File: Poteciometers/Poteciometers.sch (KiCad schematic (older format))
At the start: 14 parts, among them J1 POT_PMOD, J2 EXT_PMOD

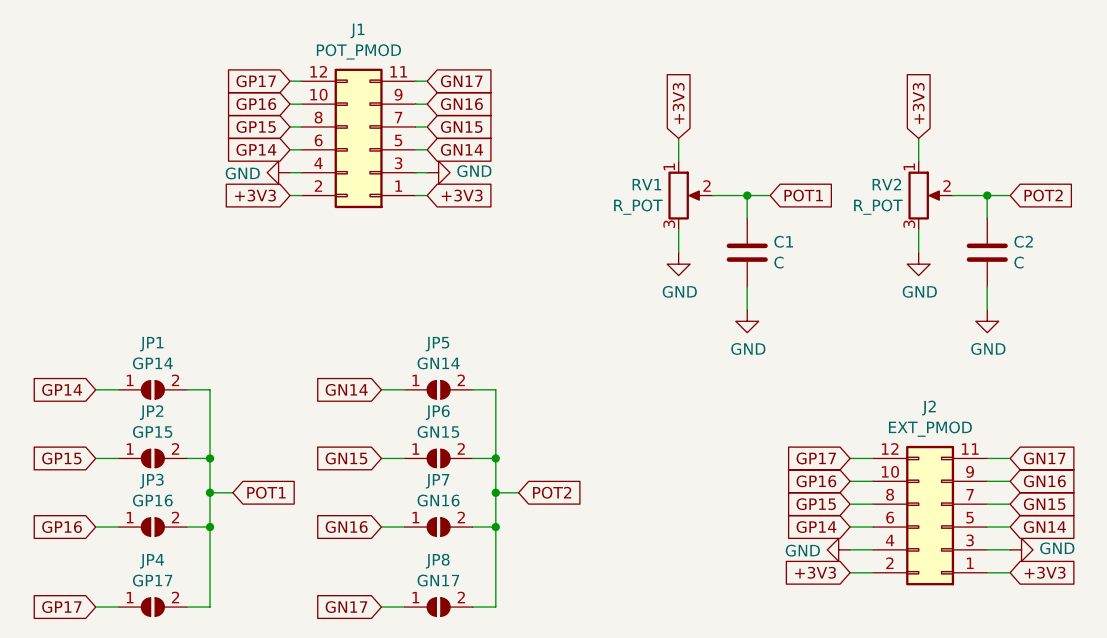
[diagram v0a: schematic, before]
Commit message: Adding shift by one suggested by tnt
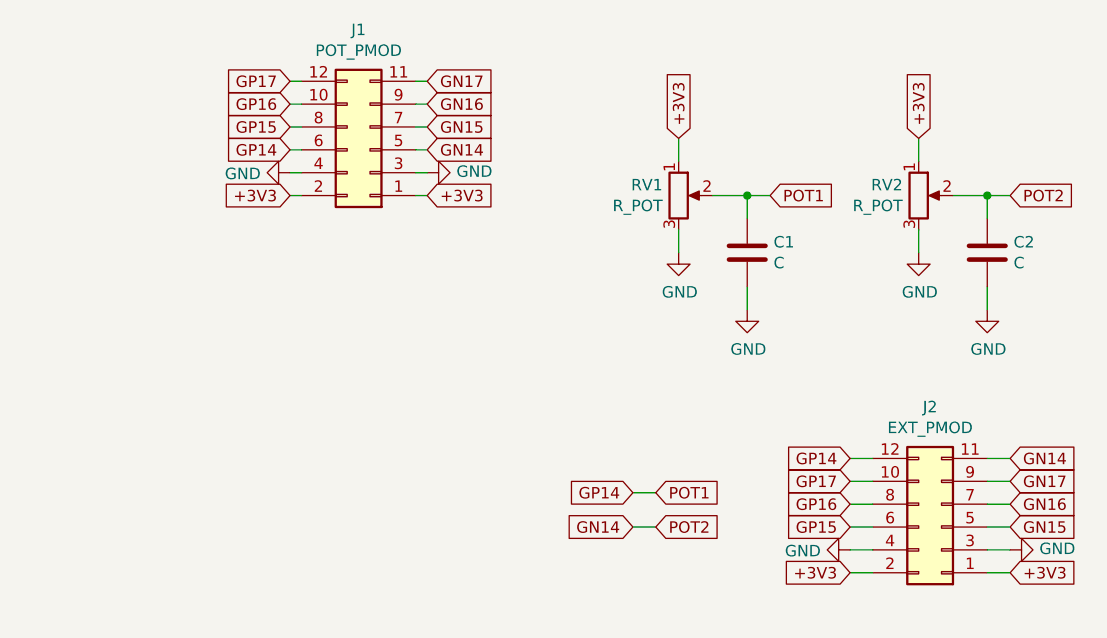
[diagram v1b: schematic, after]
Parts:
- removed JP1: GP14, Jumper:SolderJumper-2_P1.3mm_Open_TrianglePad1.0x1.5mm, symbol Jumper:SolderJumper_2_Open
- removed JP2: GP15, Jumper:SolderJumper-2_P1.3mm_Open_TrianglePad1.0x1.5mm, symbol Jumper:SolderJumper_2_Open
- removed JP3: GP16, Jumper:SolderJumper-2_P1.3mm_Open_TrianglePad1.0x1.5mm, symbol Jumper:SolderJumper_2_Open
- removed JP4: GP17, Jumper:SolderJumper-2_P1.3mm_Open_TrianglePad1.0x1.5mm, symbol Jumper:SolderJumper_2_Open
- removed JP5: GN14, Jumper:SolderJumper-2_P1.3mm_Open_TrianglePad1.0x1.5mm, symbol Jumper:SolderJumper_2_Open
- removed JP6: GN15, Jumper:SolderJumper-2_P1.3mm_Open_TrianglePad1.0x1.5mm, symbol Jumper:SolderJumper_2_Open
- removed JP7: GN16, Jumper:SolderJumper-2_P1.3mm_Open_TrianglePad1.0x1.5mm, symbol Jumper:SolderJumper_2_Open
- removed JP8: GN17, Jumper:SolderJumper-2_P1.3mm_Open_TrianglePad1.0x1.5mm, symbol Jumper:SolderJumper_2_Open
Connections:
- net POT1 is gone; now on net GP14: C1.1, RV1.2
- net POT2 is gone; now on net GN14: C2.1, RV2.2
- net GN14: now also J2.11 (Pin_11); no longer J2.5 (Pin_5)
- net GN15: now also J2.5 (Pin_5); no longer J2.7 (Pin_7)
- net GN16: now also J2.7 (Pin_7); no longer J2.9 (Pin_9)
- net GN17: now also J2.9 (Pin_9); no longer J2.11 (Pin_11)
- net GP14: now also J2.12 (Pin_12); no longer J2.6 (Pin_6)
- net GP15: now also J2.6 (Pin_6); no longer J2.8 (Pin_8)
- net GP16: now also J2.8 (Pin_8); no longer J2.10 (Pin_10)
- net GP17: now also J2.10 (Pin_10); no longer J2.12 (Pin_12)
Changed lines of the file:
@@
 Wire Wire Line
 	5100 1900 5100 1800
-$Comp
-L Jumper:SolderJumper_2_Open JP1
-U 1 1 5E8A5DA7
-P 1450 2250
-F 0 "JP1" H 1450 2455 50  0000 C CNN
-F 1 "GP14" H 1450 2364 50  0000 C CNN
-F 2 "Jumper:SolderJumper-2_P1.3mm_Open_TrianglePad1.0x1.5mm" H 1450 2250 50  0001 C CNN
-F 3 "~" H 1450 2250 50  0001 C CNN
-	1    1450 2250
-	1    0    0    -1
-$EndComp
-Text GLabel 1800 2700 2    50   Input ~ 0
+Text GLabel 3650 2700 2    50   Input ~ 0
 POT1
-$Comp
-L Jumper:SolderJumper_2_Open JP2
-U 1 1 5E8A617E
-P 1450 2550
-F 0 "JP2" H 1450 2755 50  0000 C CNN
-F 1 "GP15" H 1450 2664 50  0000 C CNN
-F 2 "Jumper:SolderJumper-2_P1.3mm_Open_TrianglePad1.0x1.5mm" H 1450 2550 50  0001 C CNN
-F 3 "~" H 1450 2550 50  0001 C CNN
-	1    1450 2550
-	1    0    0    -1
-$EndComp
-$Comp
-L Jumper:SolderJumper_2_Open JP3
-U 1 1 5E8A61A8
-P 1450 2850
-F 0 "JP3" H 1450 3055 50  0000 C CNN
-F 1 "GP16" H 1450 2964 50  0000 C CNN
-F 2 "Jumper:SolderJumper-2_P1.3mm_Open_TrianglePad1.0x1.5mm" H 1450 2850 50  0001 C CNN
-F 3 "~" H 1450 2850 50  0001 C CNN
-	1    1450 2850
-	1    0    0    -1
-$EndComp
-$Comp
-L Jumper:SolderJumper_2_Open JP4
-U 1 1 5E8A61D0
-P 1450 3200
-F 0 "JP4" H 1450 3405 50  0000 C CNN
-F 1 "GP17" H 1450 3314 50  0000 C CNN
-F 2 "Jumper:SolderJumper-2_P1.3mm_Open_TrianglePad1.0x1.5mm" H 1450 3200 50  0001 C CNN
-F 3 "~" H 1450 3200 50  0001 C CNN
-	1    1450 3200
-	1    0    0    -1
-$EndComp
-Text GLabel 1200 2250 0    50   Input ~ 0
+Text GLabel 3550 2700 0    50   Input ~ 0
 GP14
-Text GLabel 1200 2550 0    50   Input ~ 0
-GP15
-Text GLabel 1200 2850 0    50   Input ~ 0
-GP16
-Text GLabel 1200 3200 0    50   Input ~ 0
-GP17
 Wire Wire Line
-	1200 2250 1300 2250
+	3650 2700 3550 2700
+Text GLabel 3650 2850 2    50   Input ~ 0
+POT2
+Text GLabel 3550 2850 0    50   Input ~ 0
+GN14
 Wire Wire Line
-	1200 2550 1300 2550
-Wire Wire Line
-	1200 2850 1300 2850
-Wire Wire Line
-	1200 3200 1300 3200
-Wire Wire Line
-	1600 2250 1700 2250
-Wire Wire Line
-	1700 2250 1700 2550
-Wire Wire Line
-	1700 3200 1600 3200
-Wire Wire Line
-	1600 2850 1700 2850
-Connection ~ 1700 2850
-Wire Wire Line
-	1700 2850 1700 3200
-Wire Wire Line
-	1600 2550 1700 2550
-Connection ~ 1700 2550
-Wire Wire Line
-	1700 2550 1700 2700
-Wire Wire Line
-	1800 2700 1700 2700
-Connection ~ 1700 2700
-Wire Wire Line
-	1700 2700 1700 2850
-$Comp
-L Jumper:SolderJumper_2_Open JP5
-U 1 1 5E8A8F58
-P 2700 2250
-F 0 "JP5" H 2700 2455 50  0000 C CNN
-F 1 "GN14" H 2700 2364 50  0000 C CNN
-F 2 "Jumper:SolderJumper-2_P1.3mm_Open_TrianglePad1.0x1.5mm" H 2700 2250 50  0001 C CNN
-F 3 "~" H 2700 2250 50  0001 C CNN
-	1    2700 2250
-	1    0    0    -1
-$EndComp
-Text GLabel 3050 2700 2    50   Input ~ 0
-POT2
-$Comp
-L Jumper:SolderJumper_2_Open JP6
-U 1 1 5E8A8F5F
-P 2700 2550
-F 0 "JP6" H 2700 2755 50  0000 C CNN
-F 1 "GN15" H 2700 2664 50  0000 C CNN
-F 2 "Jumper:SolderJumper-2_P1.3mm_Open_TrianglePad1.0x1.5mm" H 2700 2550 50  0001 C CNN
-F 3 "~" H 2700 2550 50  0001 C CNN
-	1    2700 2550
-	1    0    0    -1
-$EndComp
-$Comp
-L Jumper:SolderJumper_2_Open JP7
-U 1 1 5E8A8F65
-P 2700 2850
-F 0 "JP7" H 2700 3055 50  0000 C CNN
-F 1 "GN16" H 2700 2964 50  0000 C CNN
-F 2 "Jumper:SolderJumper-2_P1.3mm_Open_TrianglePad1.0x1.5mm" H 2700 2850 50  0001 C CNN
-F 3 "~" H 2700 2850 50  0001 C CNN
-	1    2700 2850
-	1    0    0    -1
-$EndComp
-$Comp
-L Jumper:SolderJumper_2_Open JP8
-U 1 1 5E8A8F6B
-P 2700 3200
-F 0 "JP8" H 2700 3405 50  0000 C CNN
-F 1 "GN17" H 2700 3314 50  0000 C CNN
-F 2 "Jumper:SolderJumper-2_P1.3mm_Open_TrianglePad1.0x1.5mm" H 2700 3200 50  0001 C CNN
-F 3 "~" H 2700 3200 50  0001 C CNN
-	1    2700 3200
-	1    0    0    -1
-$EndComp
-Text GLabel 2450 2250 0    50   Input ~ 0
-GN14
-Text GLabel 2450 2550 0    50   Input ~ 0
-GN15
-Text GLabel 2450 2850 0    50   Input ~ 0
-GN16
-Text GLabel 2450 3200 0    50   Input ~ 0
-GN17
-Wire Wire Line
-	2450 2250 2550 2250
-Wire Wire Line
-	2450 2550 2550 2550
-Wire Wire Line
-	2450 2850 2550 2850
-Wire Wire Line
-	2450 3200 2550 3200
-Wire Wire Line
-	2850 2250 2950 2250
-Wire Wire Line
-	2950 2250 2950 2550
-Wire Wire Line
-	2950 3200 2850 3200
-Wire Wire Line
-	2850 2850 2950 2850
-Connection ~ 2950 2850
-Wire Wire Line
-	2950 2850 2950 3200
-Wire Wire Line
-	2850 2550 2950 2550
-Connection ~ 2950 2550
-Wire Wire Line
-	2950 2550 2950 2700
-Wire Wire Line
-	3050 2700 2950 2700
-Connection ~ 2950 2700
-Wire Wire Line
-	2950 2700 2950 2850
+	3650 2850 3550 2850
 $Comp
 L Connector_Generic:Conn_02x06_Odd_Even J2
@@
 	0    -1   -1   0
 $EndComp
+Text GLabel 4500 2550 0    50   Input ~ 0
+GP14
+Text GLabel 5200 2550 2    50   Input ~ 0
+GN14
 Text GLabel 4500 2850 0    50   Input ~ 0
-GP14
+GP15
 Text GLabel 5200 2850 2    50   Input ~ 0
-GN14
+GN15
 Text GLabel 4500 2750 0    50   Input ~ 0
-GP15
+GP16
 Text GLabel 5200 2750 2    50   Input ~ 0
-GN15
+GN16
 Text GLabel 4500 2650 0    50   Input ~ 0
-GP16
+GP17
 Text GLabel 5200 2650 2    50   Input ~ 0
-GN16
-Text GLabel 4500 2550 0    50   Input ~ 0
-GP17
-Text GLabel 5200 2550 2    50   Input ~ 0
 GN17
 Wire Wire Line
